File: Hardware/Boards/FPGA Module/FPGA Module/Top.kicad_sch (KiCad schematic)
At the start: 2 parts

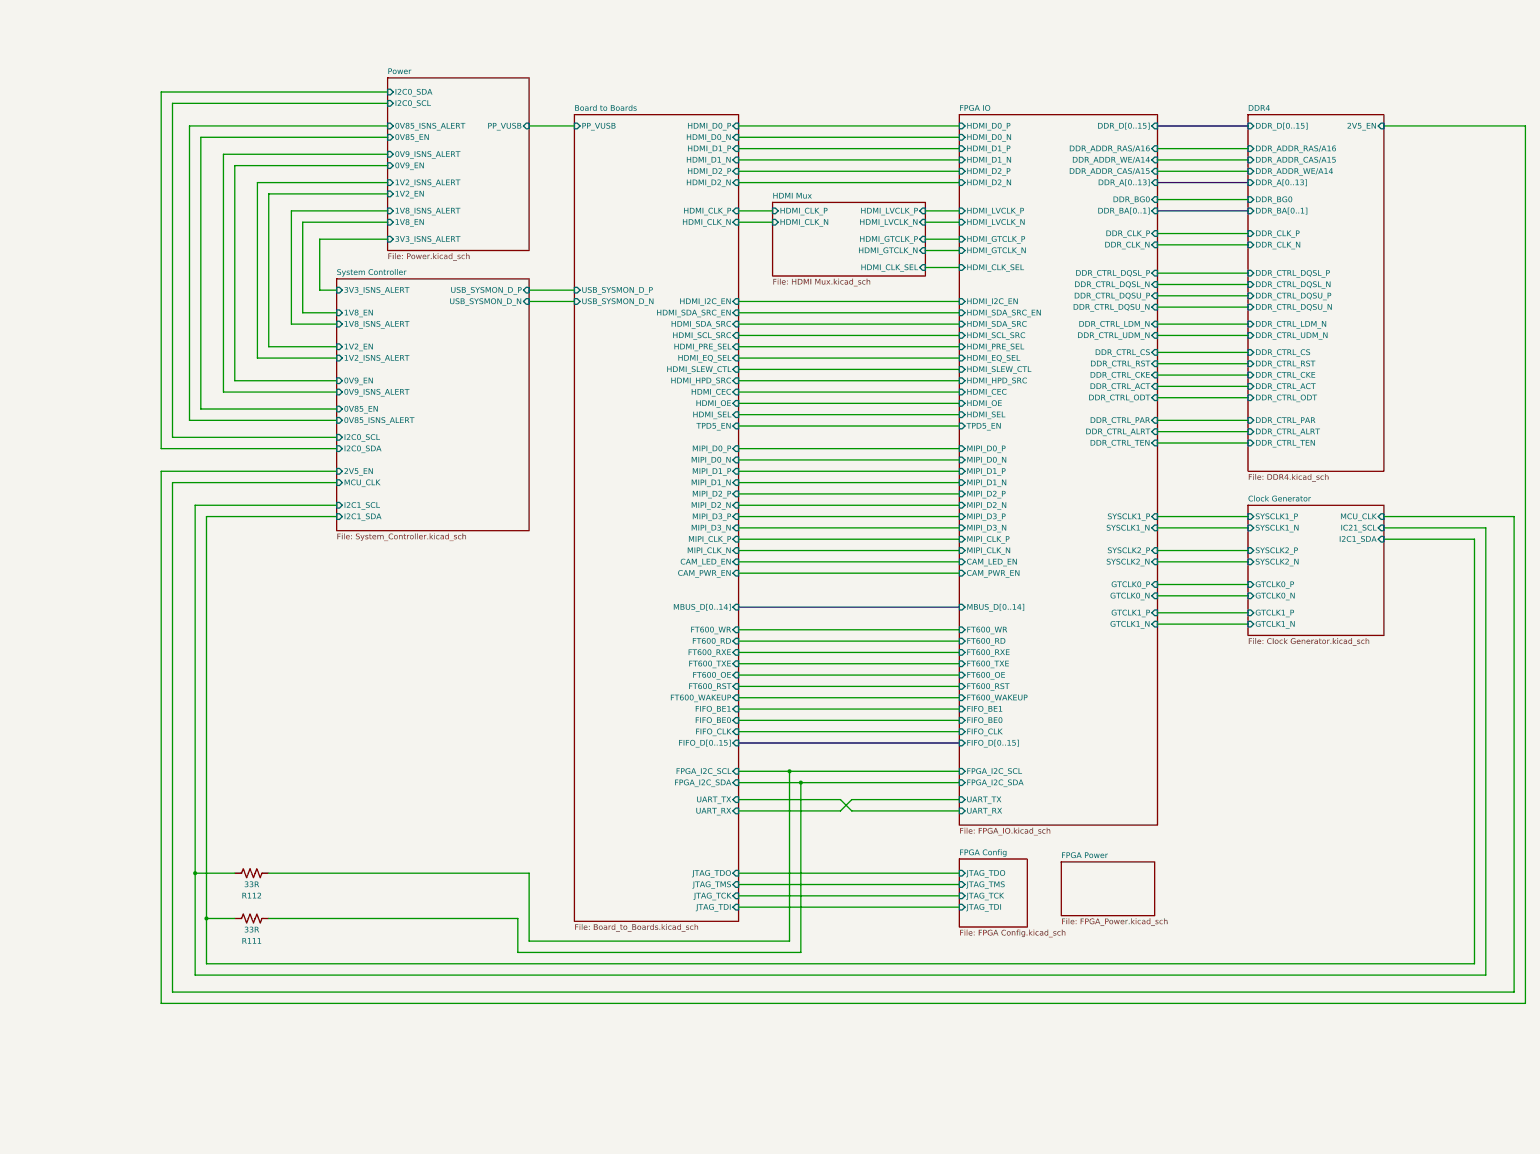
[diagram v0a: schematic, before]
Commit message: FPGA Module sch update
Added 3V3 LDO for MCU and 3V3 EN for DCDC. Also added SPI bus from MCU to FPGA with level shifter
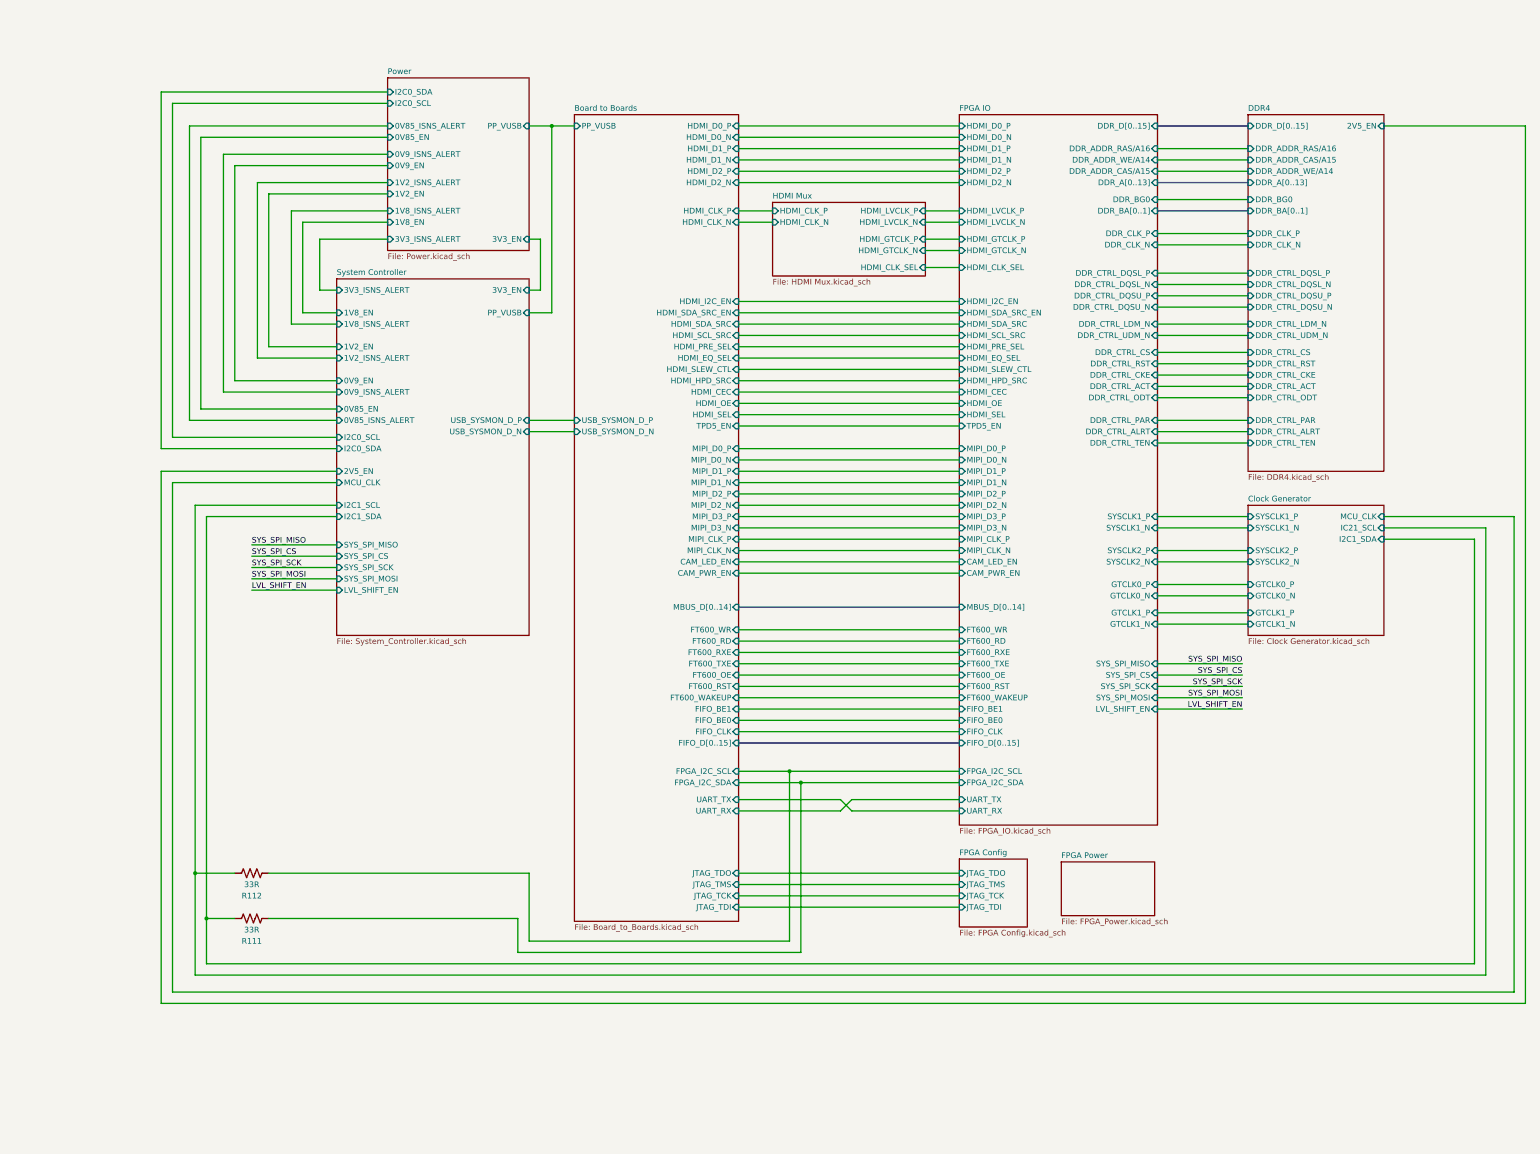
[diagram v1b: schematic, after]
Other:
- sheet FPGA IO ports: added LVL_SHIFT_EN, SYS_SPI_CS, SYS_SPI_MISO, SYS_SPI_MOSI, SYS_SPI_SCK; removed none
- sheet Power ports: added 3V3_EN; removed none
- sheet System Controller ports: added 3V3_EN, LVL_SHIFT_EN, PP_VUSB, SYS_SPI_CS, SYS_SPI_MISO, SYS_SPI_MOSI, SYS_SPI_SCK; removed none

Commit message: Completed FPGA module PCB layout
Started PCB routing
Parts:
- added TP1, TP2, TP3, TP4: Mounting Hole, MountingHole:MountingHole_2.2mm_M2_Pad_Via, symbol Connector:TestPoint
- R1: renamed from R112; footprint Resistor_SMD:R_0402_1005Metric -> Resistor_SMD:R_0201_0603Metric
- R2: renamed from R111; footprint Resistor_SMD:R_0402_1005Metric -> Resistor_SMD:R_0201_0603Metric
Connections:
- net Clock Generator/IC21_SCL renamed Clock Generator/I2C1_SCL
- new net GND: TP1.1, TP2.1, TP3.1, TP4.1
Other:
- sheet Clock Generator ports: added I2C1_SCL; removed IC21_SCL
- sheet Power ports: added 3V3_AON; removed none
- sheet System Controller ports: added 3V3_AON; removed PP_VUSB

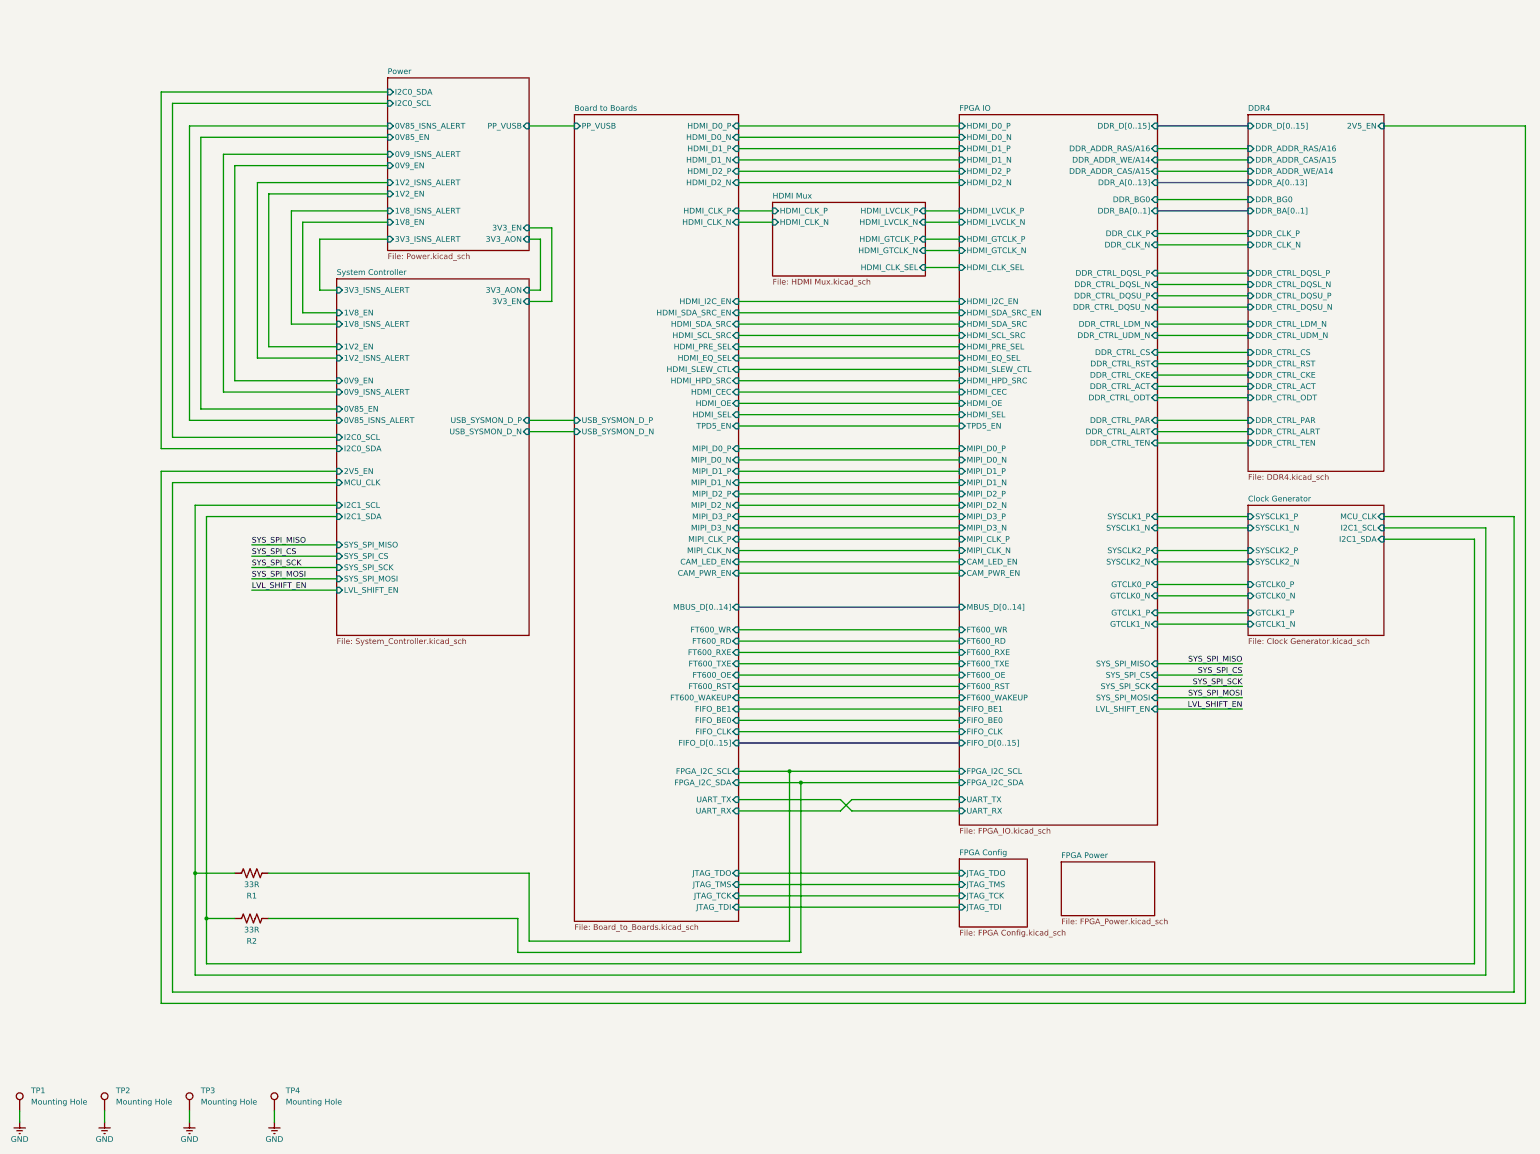
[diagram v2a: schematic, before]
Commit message: Updated SCH and Layout
Added temp sensors for DCDC's, Added MCU control for FPGA mode, removed mode DIP switch
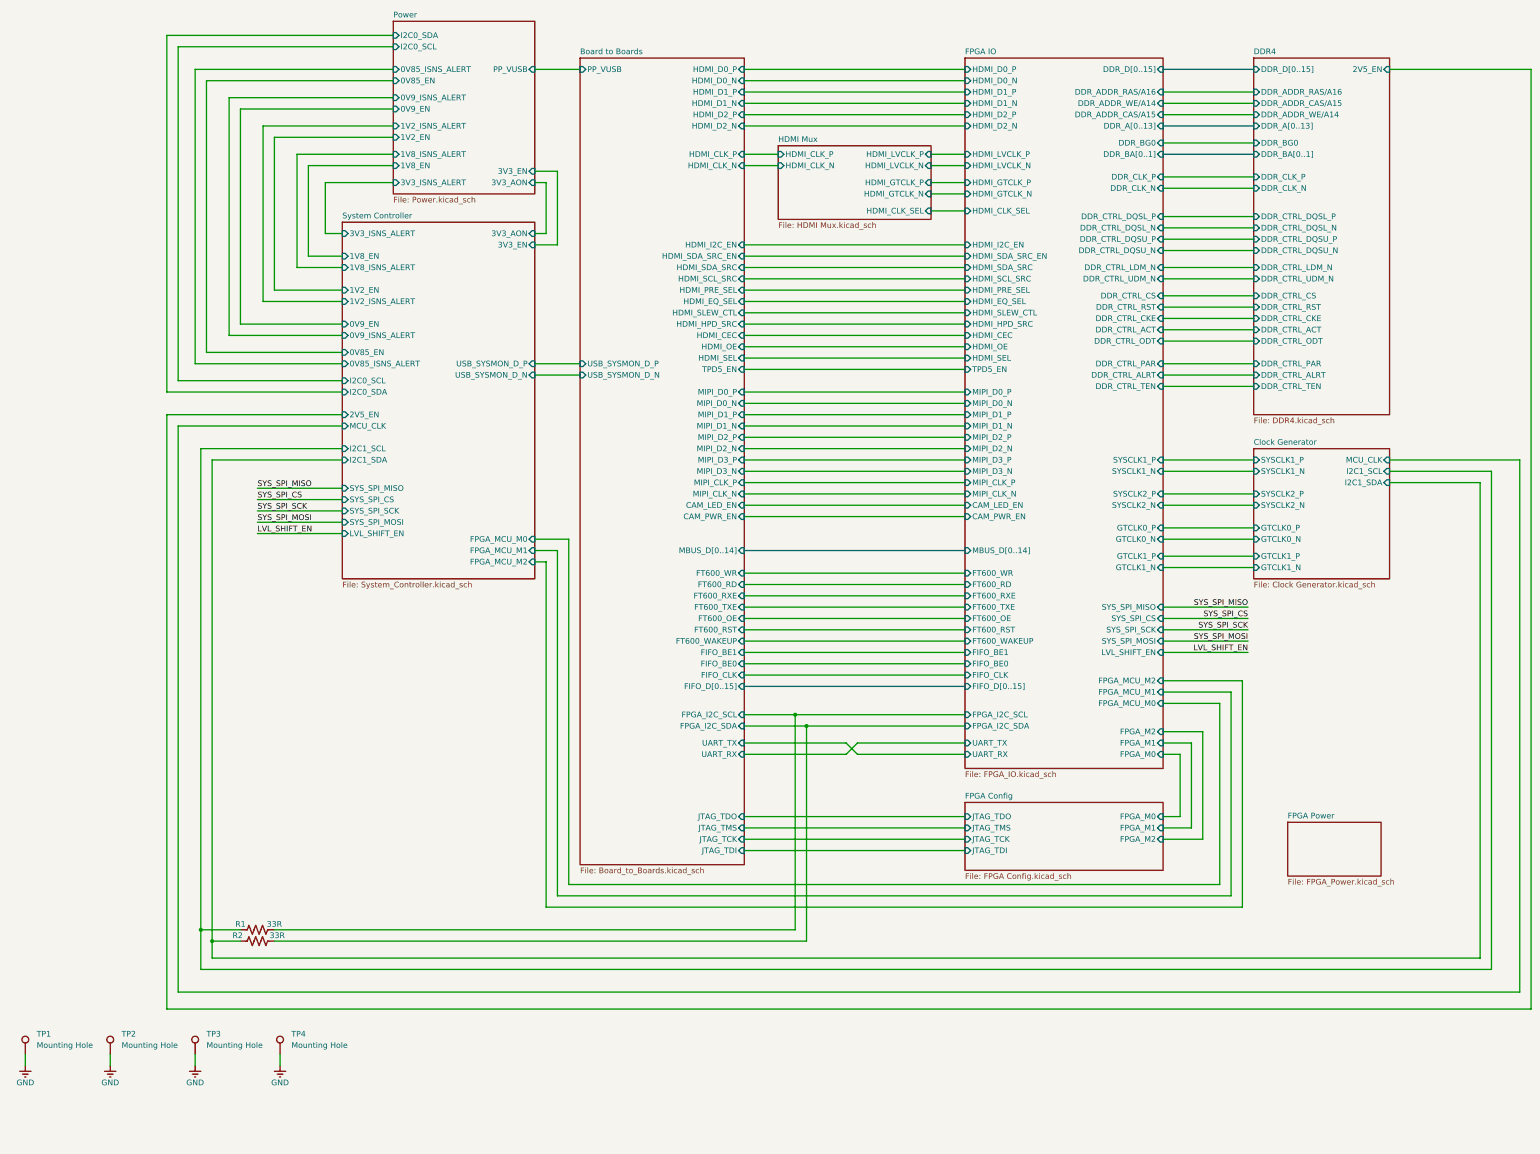
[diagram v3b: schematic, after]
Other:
- sheet FPGA Config ports: added FPGA_M0, FPGA_M1, FPGA_M2; removed none
- sheet FPGA IO ports: added FPGA_M0, FPGA_M1, FPGA_M2, FPGA_MCU_M0, FPGA_MCU_M1, FPGA_MCU_M2; removed none
- sheet System Controller ports: added FPGA_MCU_M0, FPGA_MCU_M1, FPGA_MCU_M2; removed none
- moved on the sheet: R1, R2, TP1, TP2, TP3, TP4
